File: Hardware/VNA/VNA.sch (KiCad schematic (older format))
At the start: 28 parts, among them J1 USB_B_Micro, J2 USB_A, J3 Conn_ARM_SWD, J4 SMA, J5 SMA, J6 UART, U1 TPD2S017, U2 TPD2S017

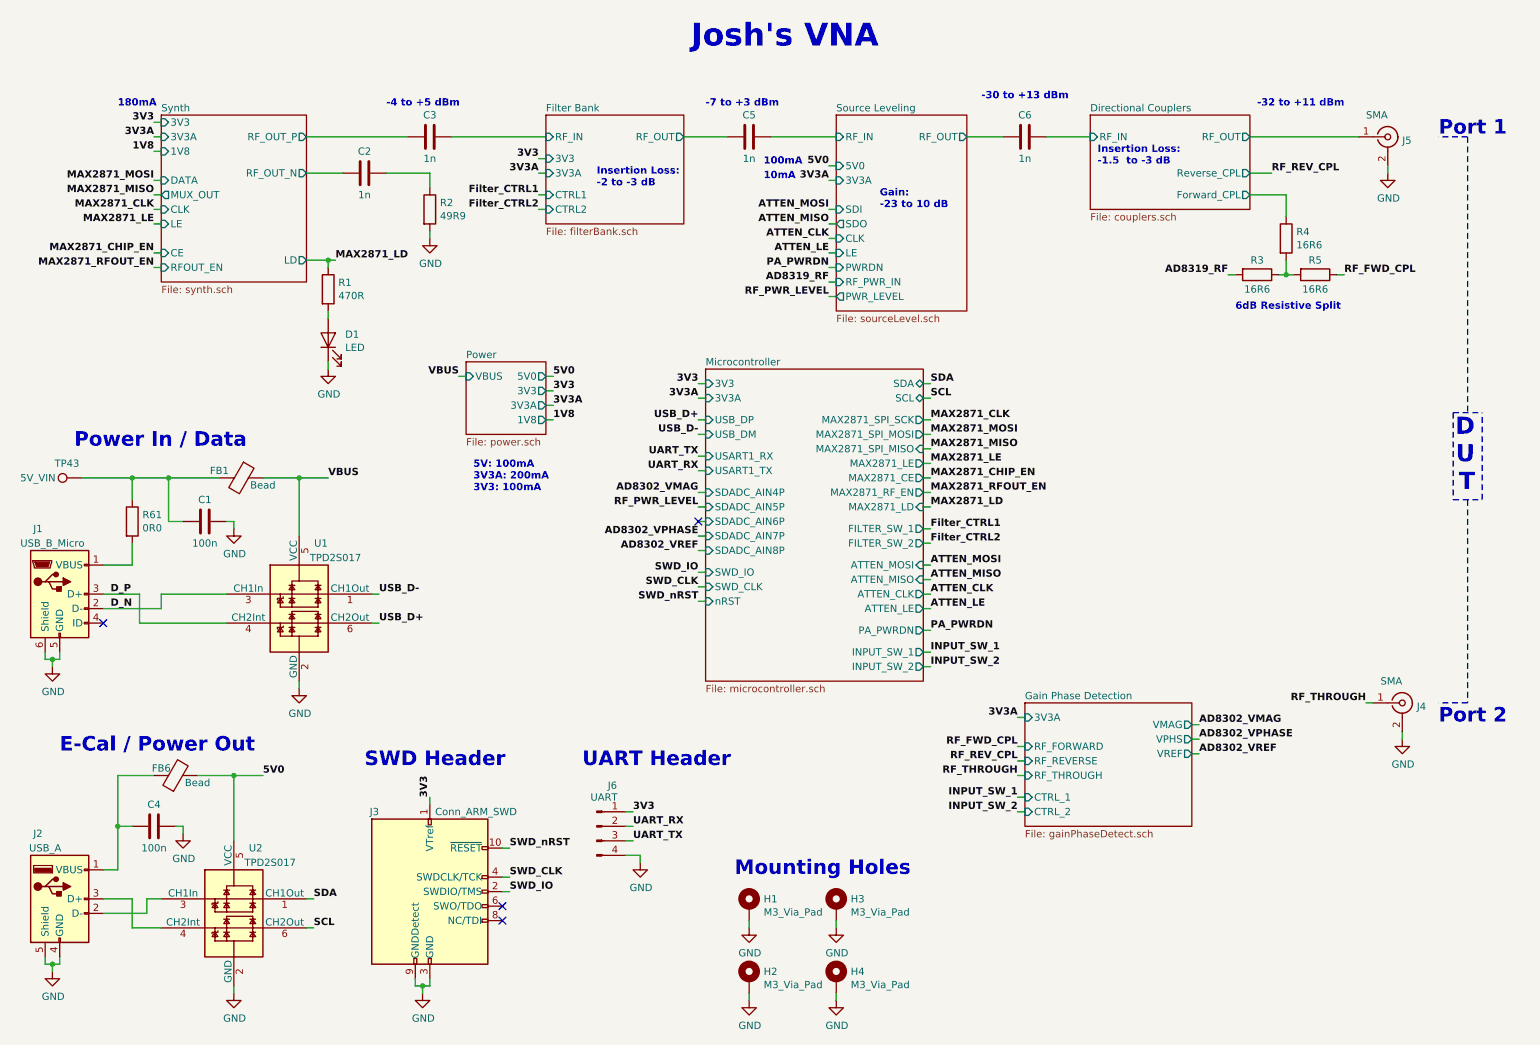
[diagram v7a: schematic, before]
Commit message: fix KiCad 5.1.0 bold after plot issue on schematics
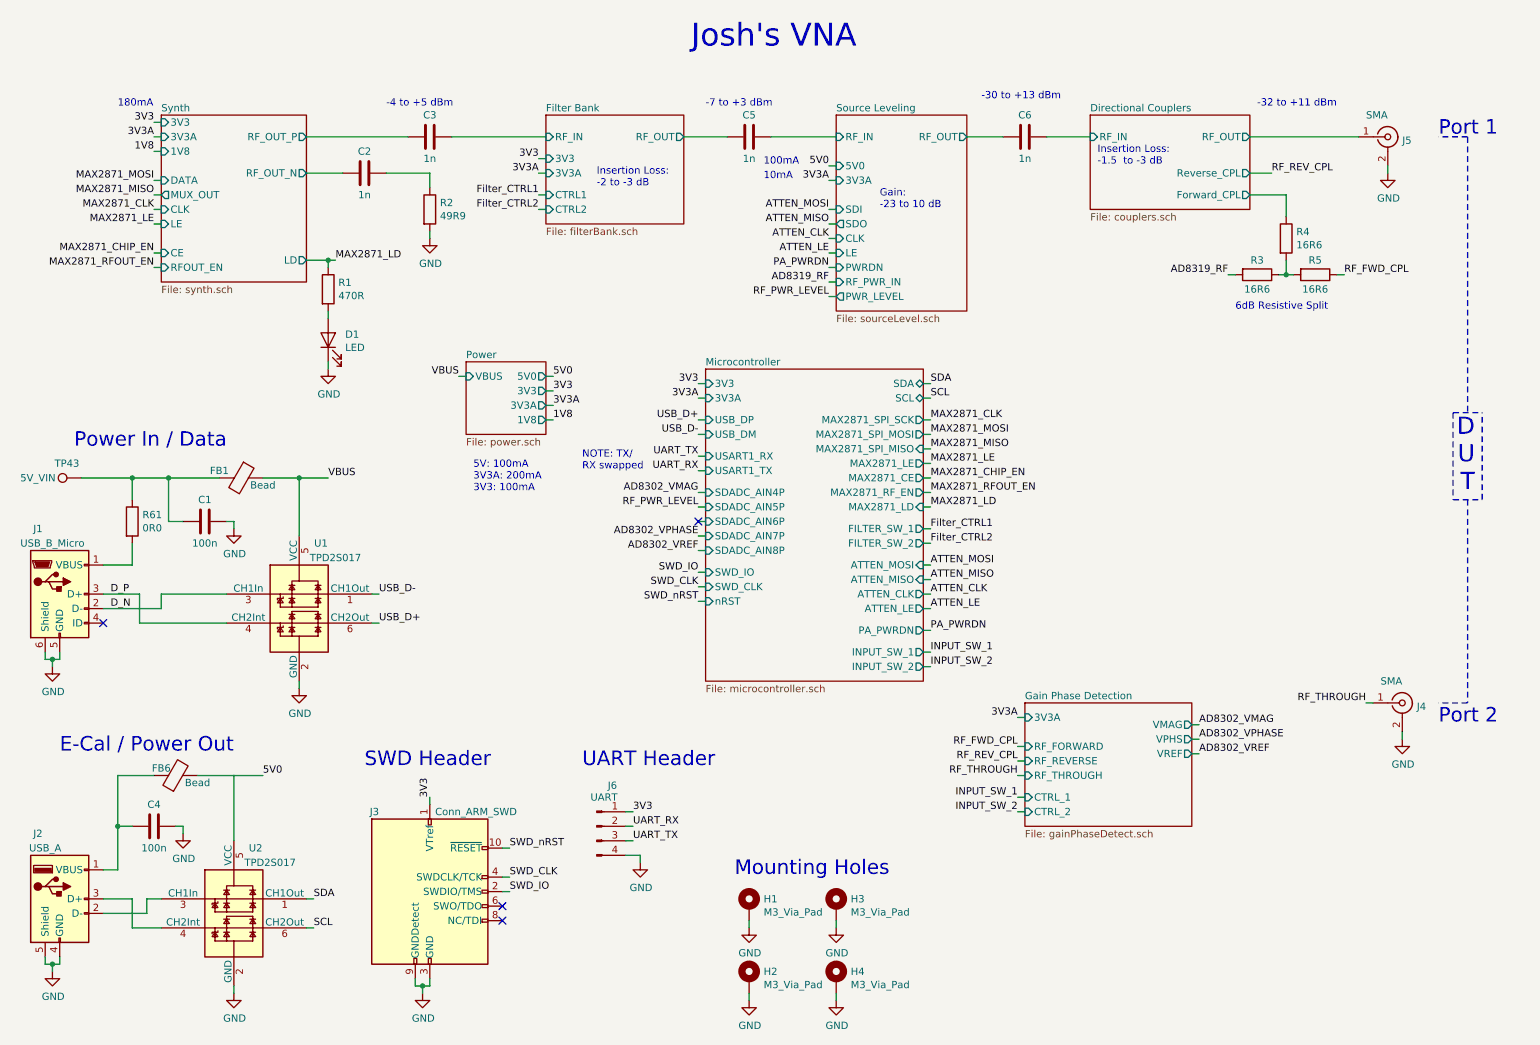
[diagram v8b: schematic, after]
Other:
- note added: "NOTE: TX/\nRX swapped"
